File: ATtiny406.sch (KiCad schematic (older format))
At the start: 14 parts, among them J1 Conn_01x06_Male, J2 Conn_01x10_Male, J3 Conn_01x10_Male, SW1 SW_Push, U1 ATtiny406-S

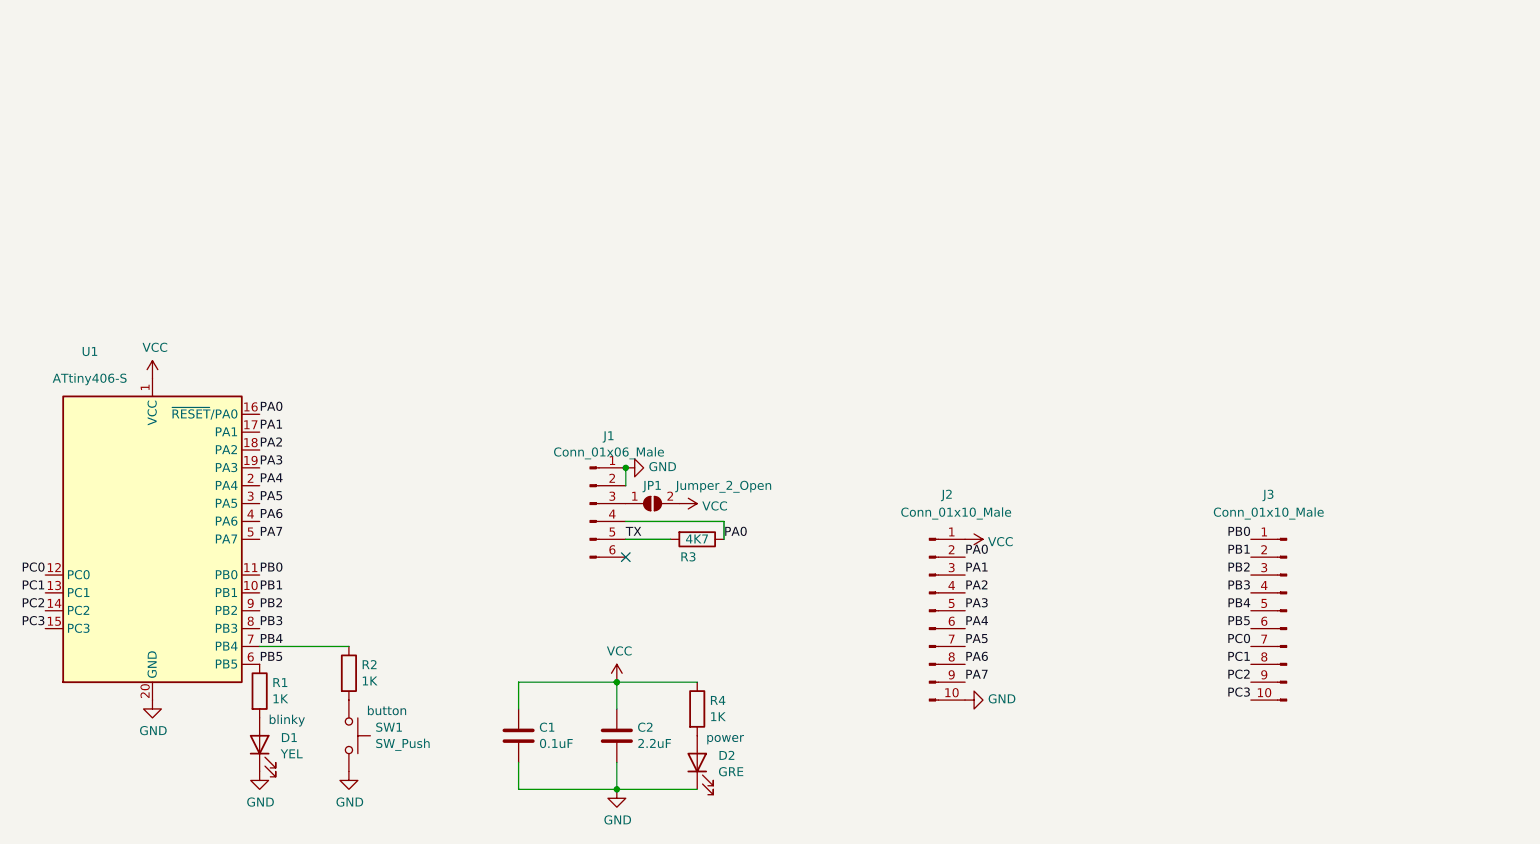
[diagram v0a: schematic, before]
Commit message: Revision 1 Release
Revision 1 changes: Changed PA0 from J1 pin 4 to pin 5.
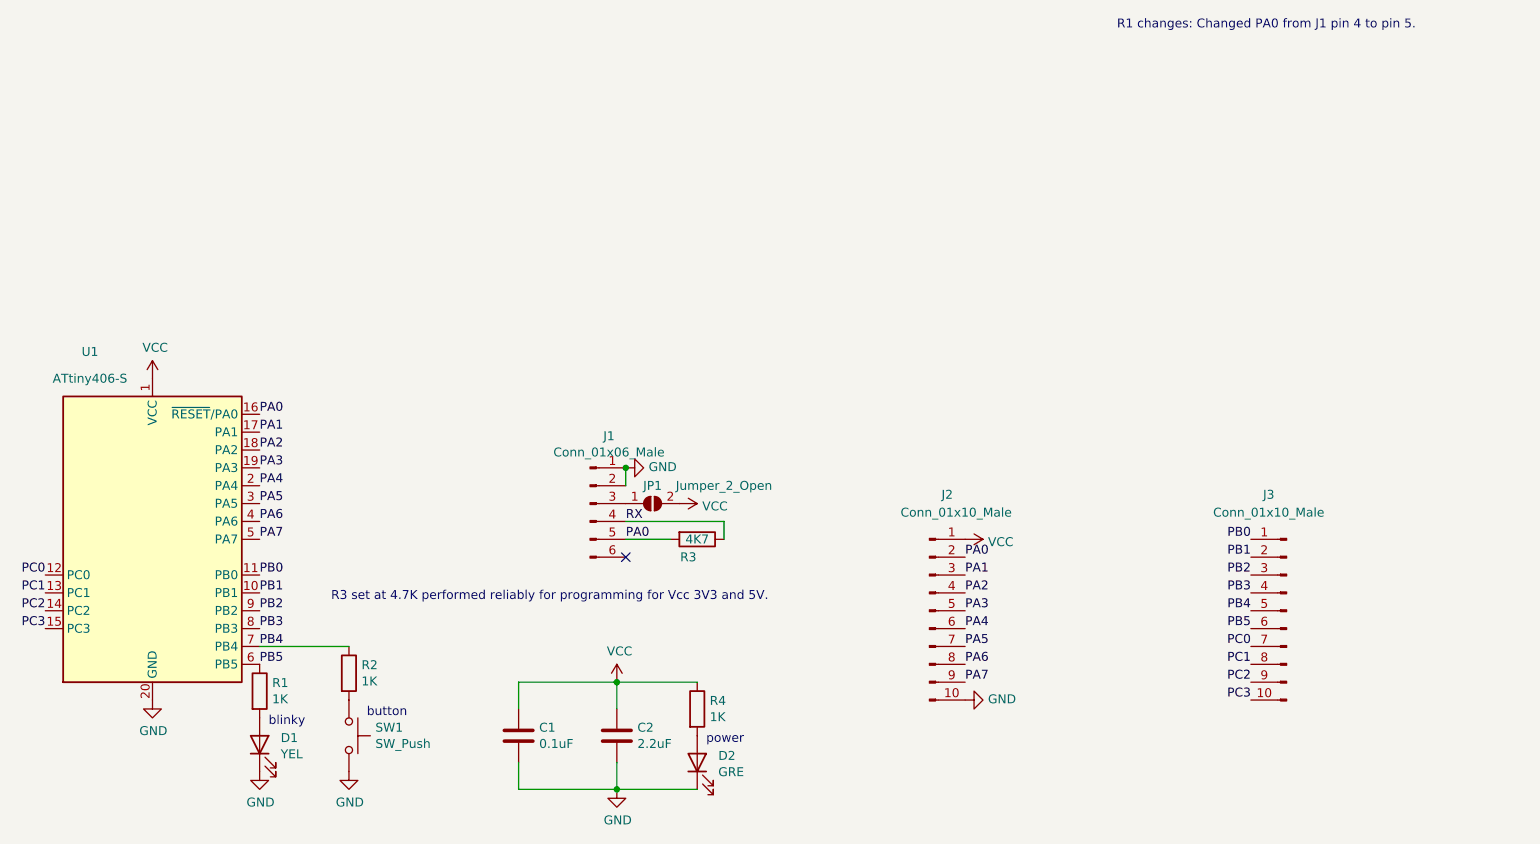
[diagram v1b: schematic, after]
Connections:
- net TX is gone; now on net PA0: J1.5 (Pin_5), R3.2
- net PA0: no longer J1.4 (Pin_4), R3.1
- new net RX: J1.4 (Pin_4), R3.1
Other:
- note added: "R1 changes: Changed PA0 from J1 pin 4 to pin 5."
- note added: "R3 set at 4.7K performed reliably for programming for Vcc 3V3 and 5V."
